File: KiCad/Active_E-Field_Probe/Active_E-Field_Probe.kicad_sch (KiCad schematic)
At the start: 16 parts

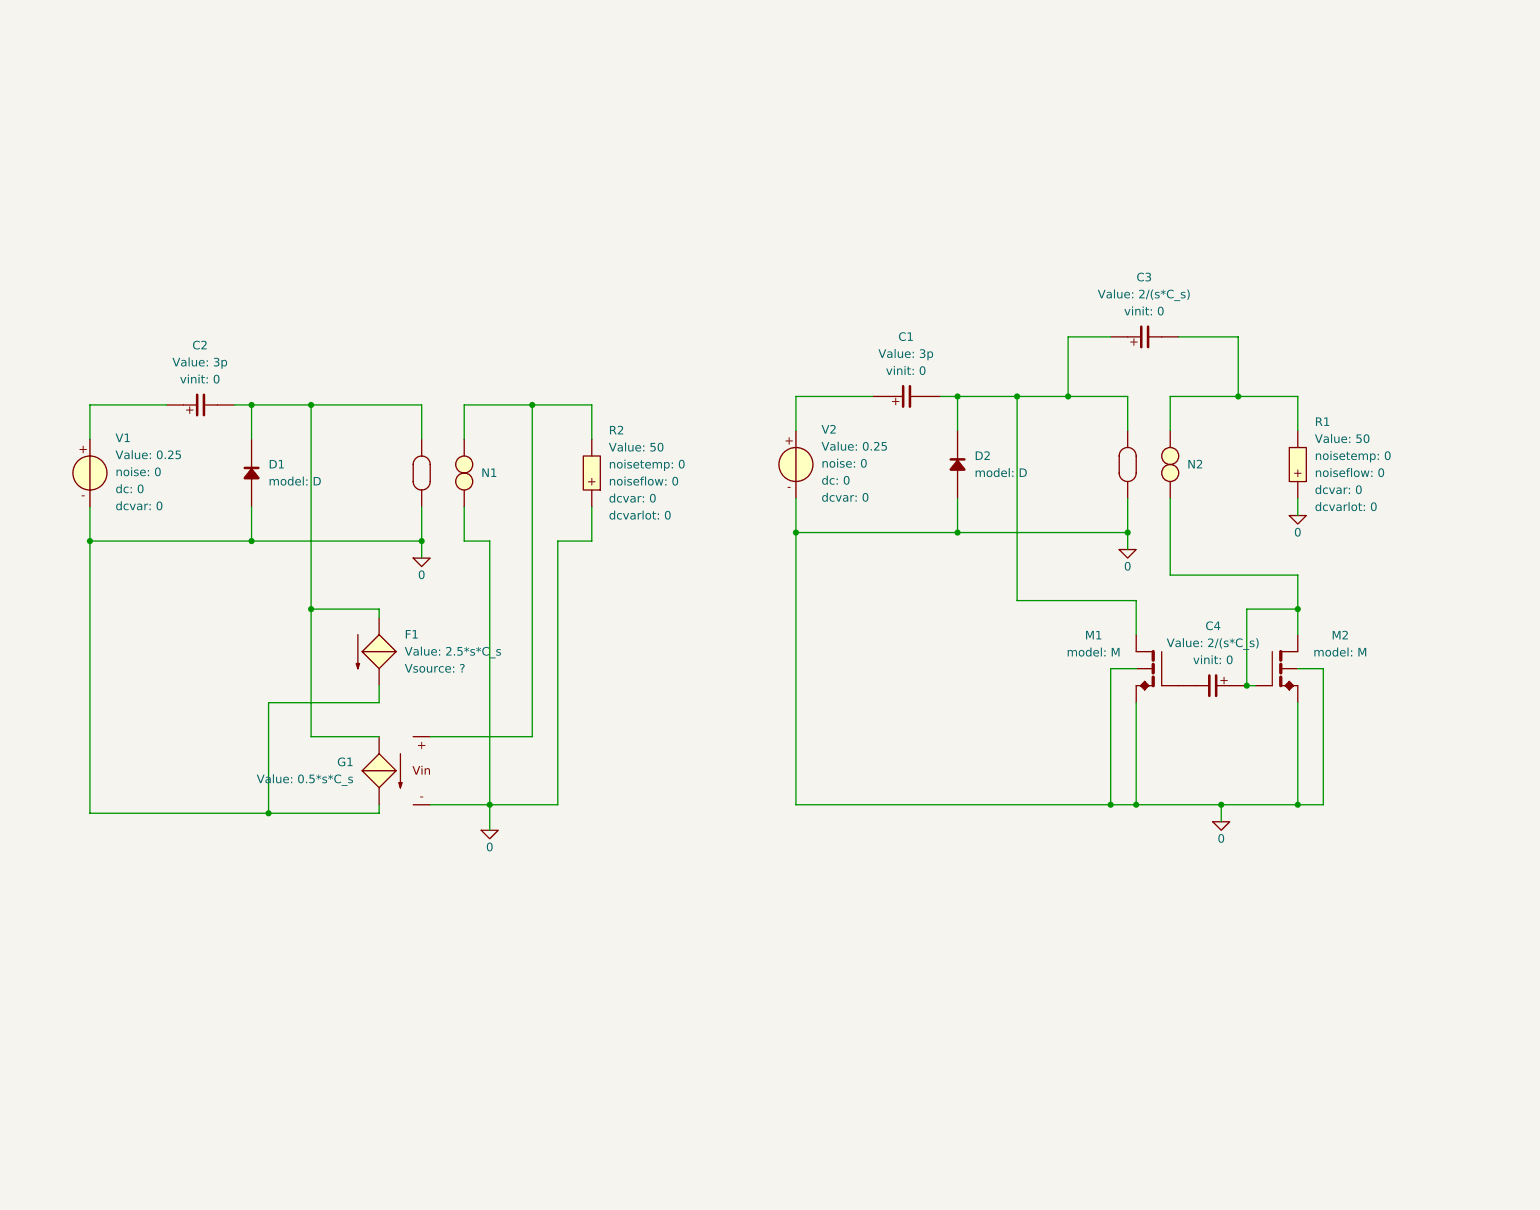
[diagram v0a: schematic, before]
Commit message: Added Specifications Page
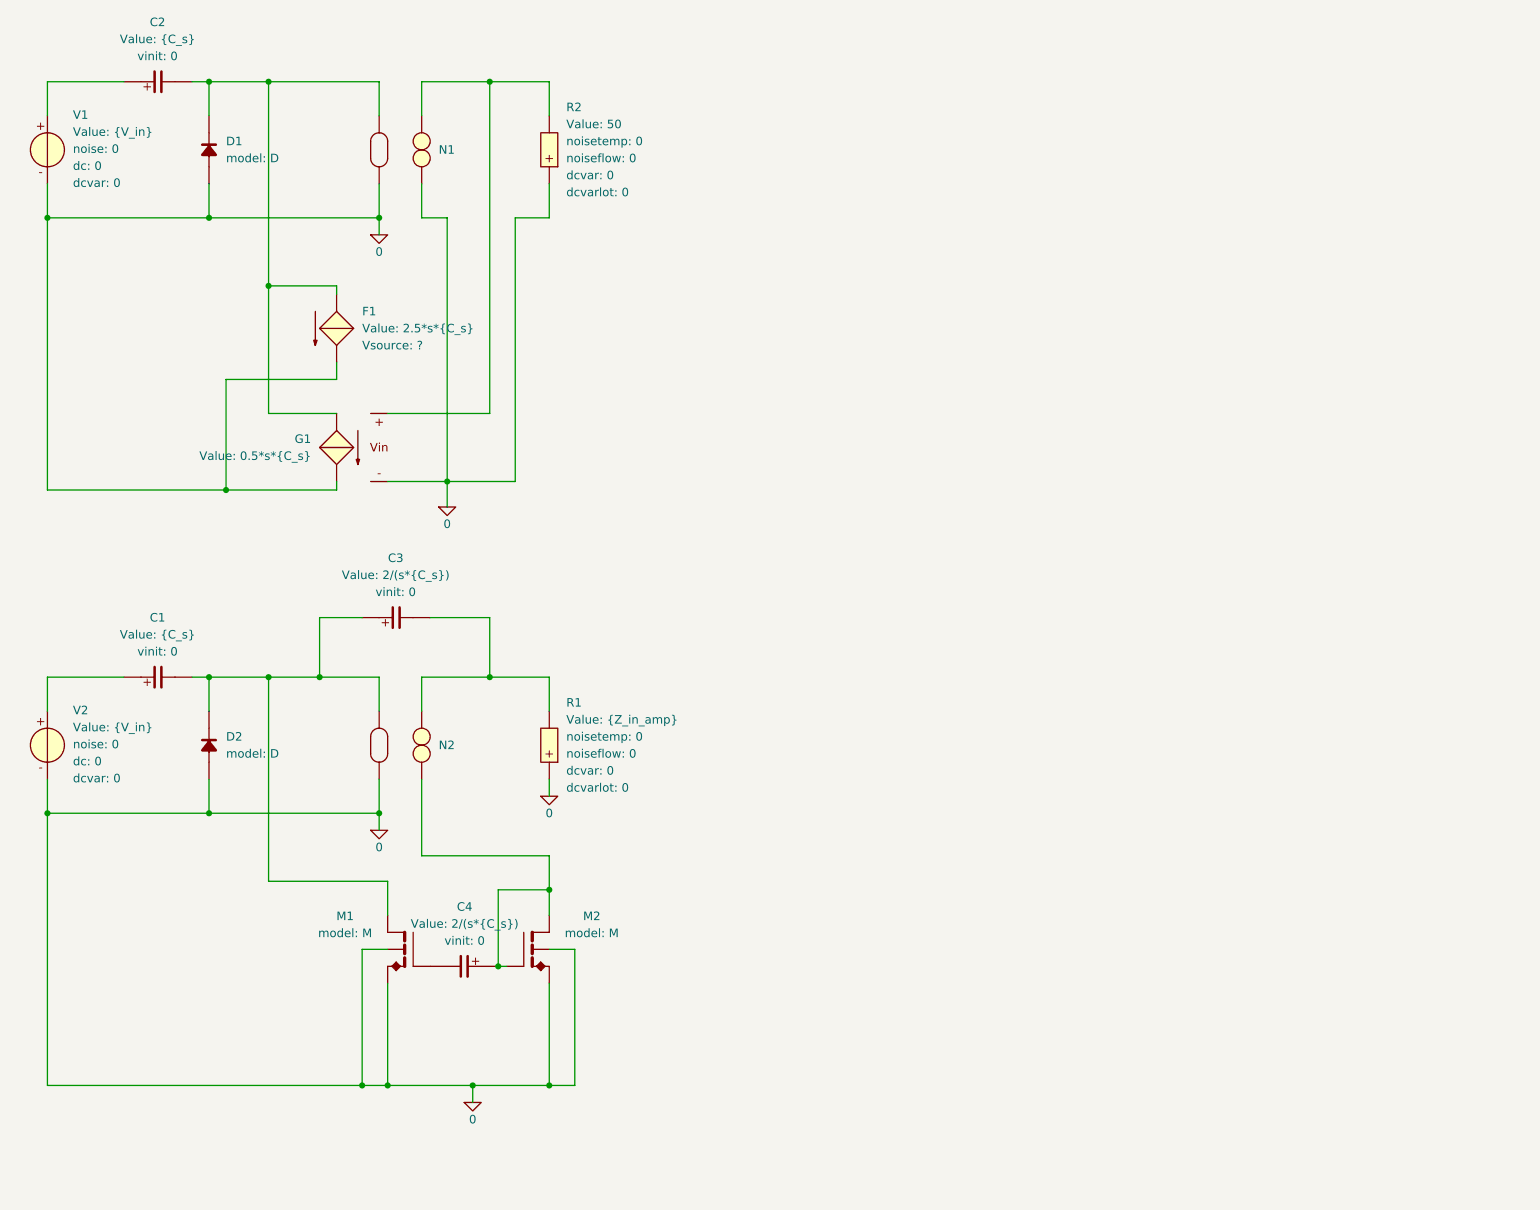
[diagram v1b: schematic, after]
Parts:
- C1, C2: value 3p -> {C_s}
- C3, C4: value 2/(s*C_s) -> 2/(s*{C_s})
- F1: value 2.5*s*C_s -> 2.5*s*{C_s}
- G1: value 0.5*s*C_s -> 0.5*s*{C_s}
- R1: value 50 -> {Z_in_amp}
- V1, V2: value 0.25 -> {V_in}
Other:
- moved on the sheet: C1, C2, C3, C4, D1, D2, F1, G1, M1, M2, N1, N2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

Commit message: meeting 18-09
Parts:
- added C5: {C_s}, symbol SLiCAP:C
- added C6, C7: 2/(s*{C_s}), symbol SLiCAP:C
- added D3: ~, symbol SLiCAP:D
- added M3, M4: ~, symbol SLiCAP:M
- added N3: ~, symbol SLiCAP:N
- added R3: 50, symbol SLiCAP:R
- added V3: {V_in}, symbol SLiCAP:V
- added X1: ~, symbol SLiCAP:Xio4
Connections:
- net 0: now also C3.1, R2.2, C6.2, M3.1 (D), N3.1 (outP), N3.3 (inp), N3.4 (inN); no longer M1.3 (S), M1.4 (B), M2.3 (S), M2.4 (B), R2.1
- net at C1.2, D2.2, M1.1 (D)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: no longer C3.1
- net at G1.3 (inp), N1.1 (outP): now also R2.1; no longer R2.2
- net at C1.1, V2.1 (p): now also C6.1
- new net: C7.1, M4.1 (D), M4.2 (G), N3.2 (outN)
- new net: C5.1, V3.1 (p)
- new net: C5.2, D3.2, X1.1 (inP)
- new net: C7.2, M3.2 (G)
- new net: D3.1, V3.2 (n), X1.2 (inN)
- new net: R3.1, X1.3 (outP)
- new net: R3.2, X1.4 (outN)
- new net: M1.3 (S), M1.4 (B), M2.3 (S), M2.4 (B), M3.3 (S), M3.4 (B), M4.3 (S), M4.4 (B)
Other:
- moved on the sheet: C1, C2, C3, C4, D1, D2, F1, G1, M1, M2, N1, N2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

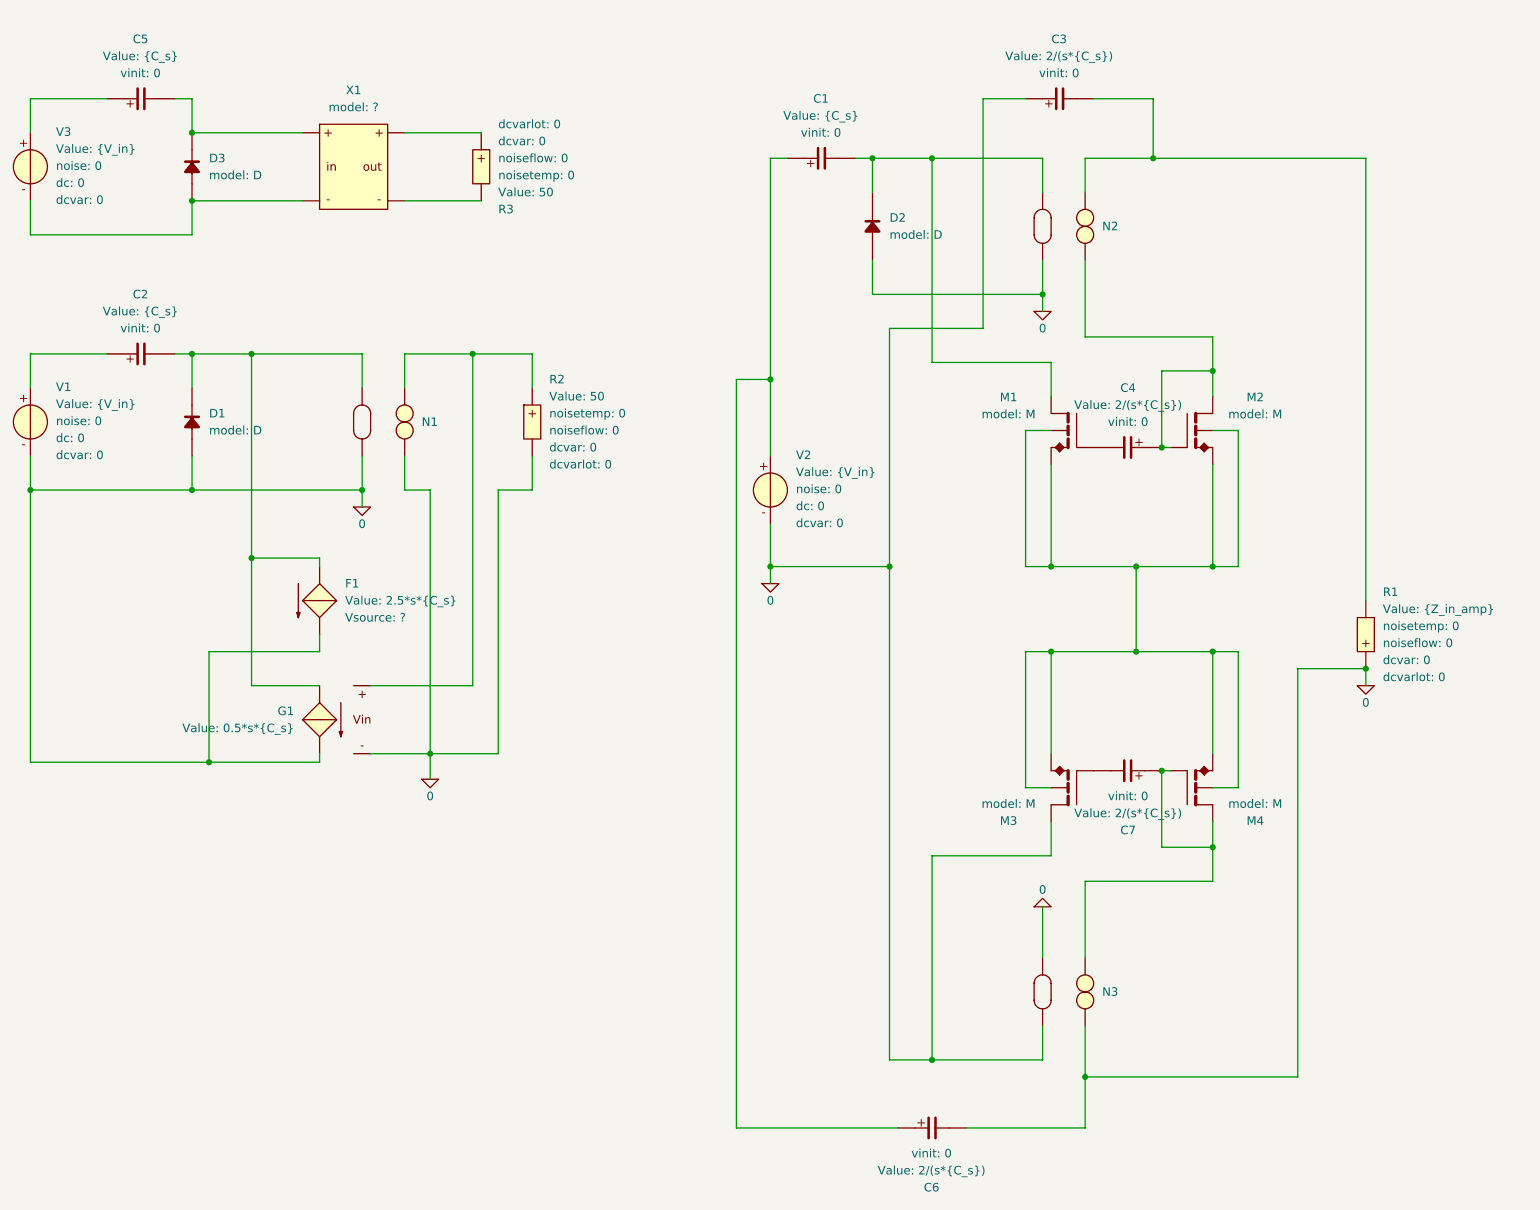
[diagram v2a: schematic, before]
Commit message: cleanup of schematics
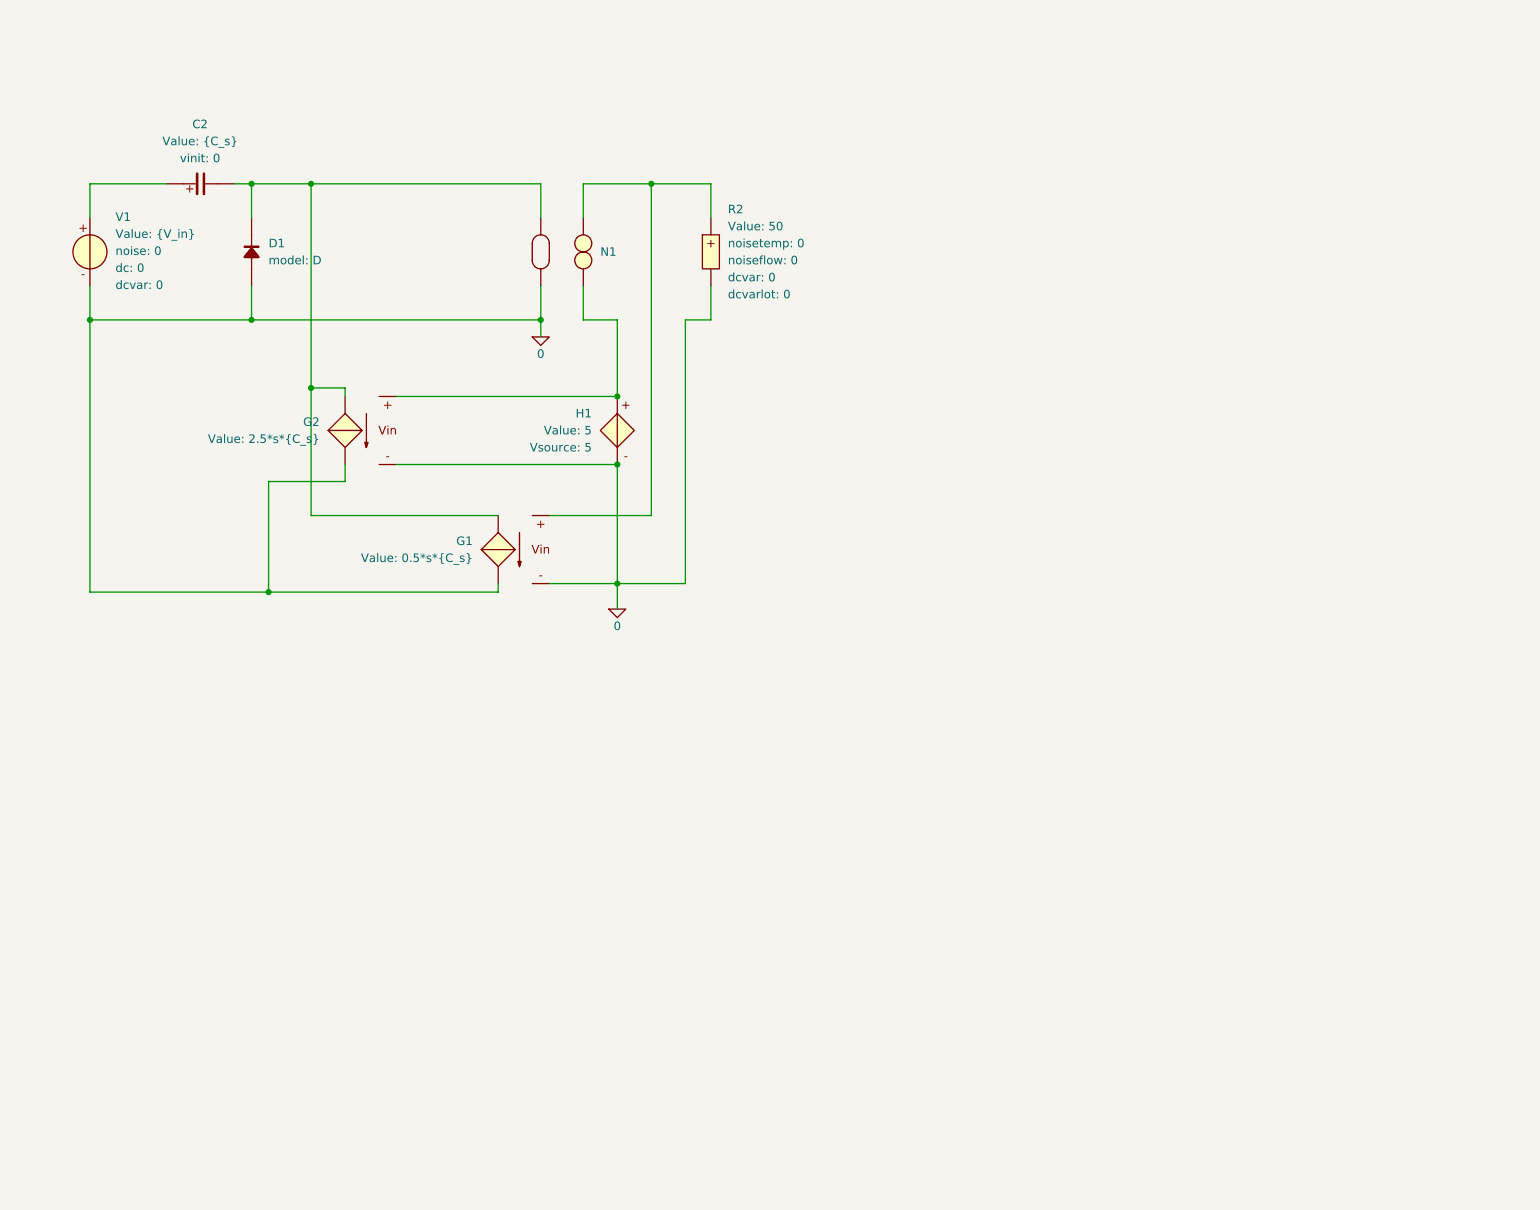
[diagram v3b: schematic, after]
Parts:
- removed C1, C5: {C_s}, symbol SLiCAP:C
- removed C3, C4, C6, C7: 2/(s*{C_s}), symbol SLiCAP:C
- removed D2, D3: ~, symbol SLiCAP:D
- removed F1: 2.5*s*{C_s}, symbol SLiCAP:F
- removed M1, M2, M3, M4: ~, symbol SLiCAP:M
- removed N2, N3: ~, symbol SLiCAP:N
- removed R1: {Z_in_amp}, symbol SLiCAP:R
- removed R3: 50, symbol SLiCAP:R
- removed V2, V3: {V_in}, symbol SLiCAP:V
- removed X1: ~, symbol SLiCAP:Xio4
- added G2: 2.5*s*{C_s}, symbol SLiCAP:G
- added H1: 5, symbol SLiCAP:H
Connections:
- net 0: now also G2.2 (outN), G2.4 (inN), H1.2 (outN); no longer N1.2 (outN)
- net at C2.2, D1.2, G1.1 (p)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: now also G2.1 (p)
- new net: G2.3 (inp), H1.1 (outP), N1.2 (outN)
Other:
- moved on the sheet: C2, D1, G1, N1, R2, V1
